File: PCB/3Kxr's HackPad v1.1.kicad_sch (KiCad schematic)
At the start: 7 parts, among them SW1 SW_Push, SW2 SW_Push, SW3 SW_Push, SW4 SW_Push, U1 XIAO-RP2040-DIP

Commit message: update HackPad v1.1
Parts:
- added SW8: RotaryEncoder_Switch, Rotary_Encoder:RotaryEncoder_Alps_EC11E-Switch_Vertical_H20mm, symbol Device:RotaryEncoder_Switch
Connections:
- net GND: now also SW8.C
- net at SW3.2, U1.10 (GPIO4/MISO): now also SW8.S1
- net at SW4.2, U1.11 (GPIO3/MOSI): now also SW8.S2
- net at SW1.2, U1.8 (GPIO1/RX): now also SW8.A
- net at SW2.2, U1.9 (GPIO2/SCK): now also SW8.B
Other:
- moved on the sheet: D1, D2, SW1, SW2, SW3, SW4, U1

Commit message: update HackPad v1.1
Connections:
- net GND: now also SW8.S1
- net at U1.1 (GPIO26/ADC0/A0): now also SW8.A
- net at SW3.2, U1.10 (GPIO4/MISO): no longer SW8.S1
- net at SW4.2, U1.11 (GPIO3/MOSI): no longer SW8.S2
- net at U1.2 (GPIO27/ADC1/A1): now also SW8.B
- net at U1.3 (GPIO28/ADC2/A2): now also SW8.S2
- net at SW1.2, U1.8 (GPIO1/RX): no longer SW8.A
- net at SW2.2, U1.9 (GPIO2/SCK): no longer SW8.B

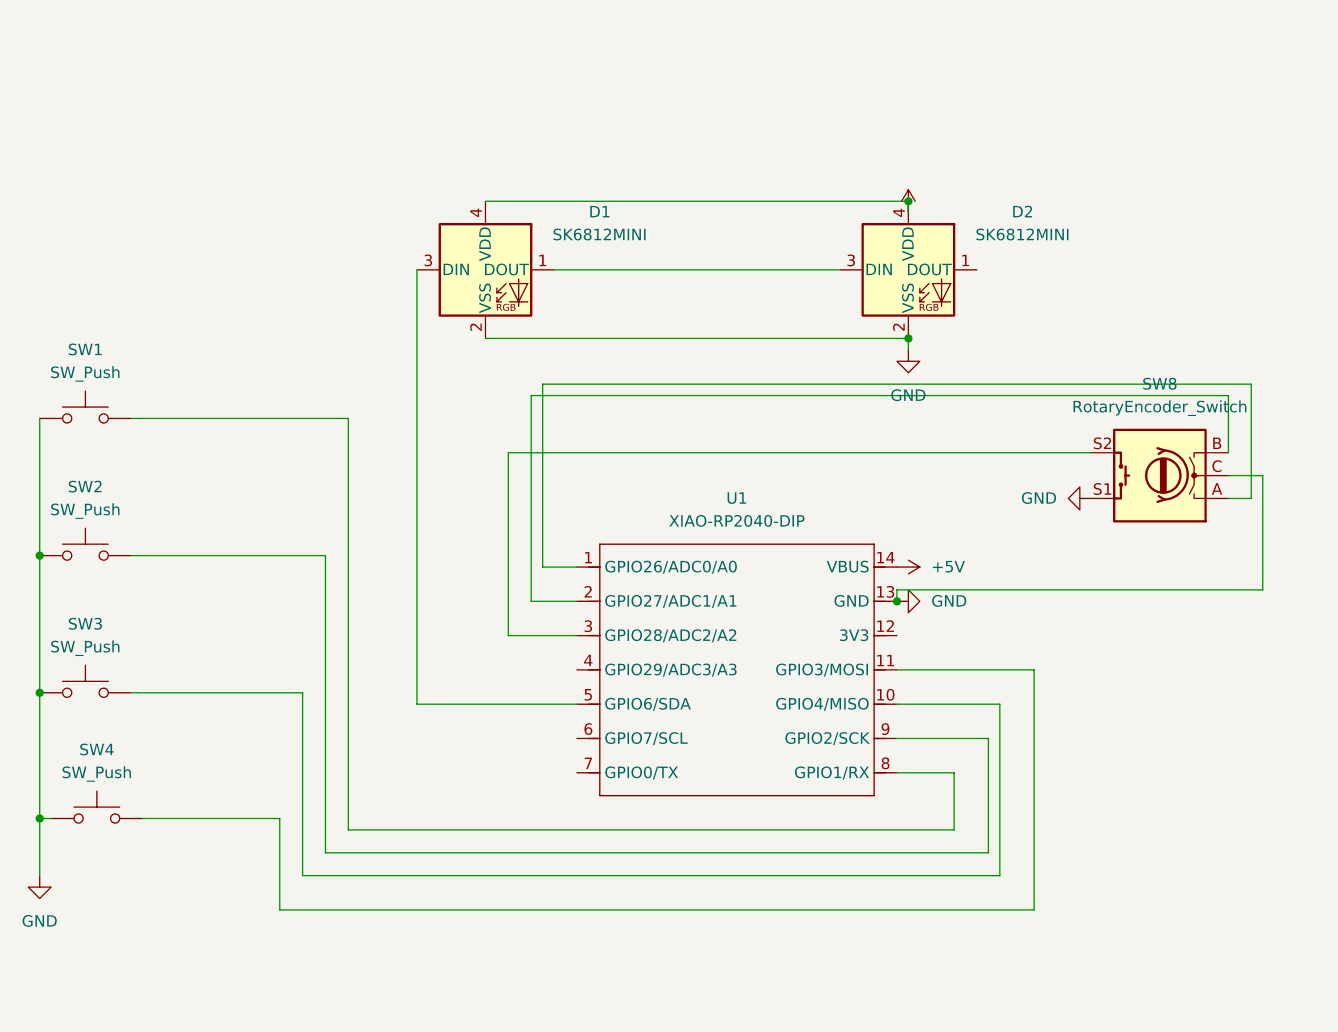
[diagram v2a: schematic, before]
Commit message: refactor: replace SK6812MINI with SK6812MINI-E and reorganize the circuit
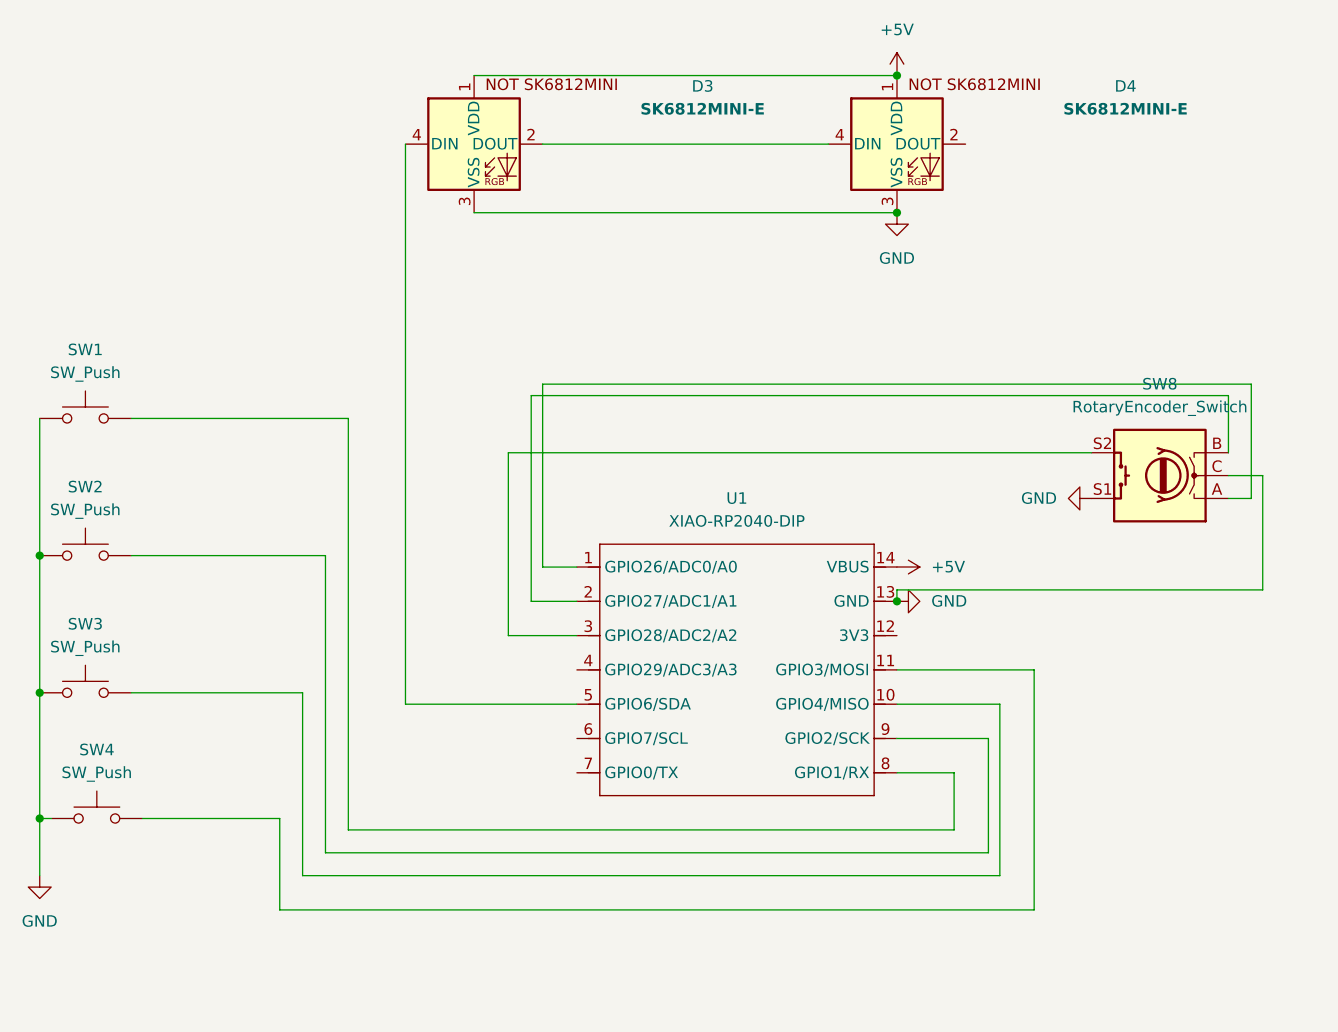
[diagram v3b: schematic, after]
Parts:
- removed D1, D2: SK6812MINI, LED_SMD:LED_SK6812MINI_PLCC4_3.5x3.5mm_P1.75mm, symbol LED:SK6812MINI
- added D3, D4: SK6812MINI-E, SK6812MINI-E:SK6812MINI-E_fixed, symbol SK6812MINI-E:SK6812MINI-E
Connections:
- net +5V: now also D3.1 (VDD), D4.1 (VDD)
- net GND: now also D3.3 (VSS), D4.3 (VSS)
- net at U1.5 (GPIO6/SDA): now also D3.4 (DIN)
- new net: D3.2 (DOUT), D4.4 (DIN)
